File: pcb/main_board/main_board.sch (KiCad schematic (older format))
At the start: 32 parts, among them J1 Sensors_Conn, J2 Power_Conn, J3 I2C_Conn, J4 Garage_Conn, J5 Debug_Sensors_Conn, J6 Debug_I2C_Conn, U1 ESP-01, U2 HC_05, U3 AT24CS64-SSHM, U4 AMS1117-3.3, U5 Black_Pill

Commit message: PCB layout added
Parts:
- U1: footprint Connector_PinHeader_2.54mm:PinHeader_2x04_P2.54mm_Vertical -> project_footprints:ESP01
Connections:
- net DHT_SENSOR1: now also J1.6 (Pin_6), J5.6 (Pin_6); no longer J1.2 (Pin_2), J5.2 (Pin_2)
- net DHT_SENSOR2: now also J1.7 (Pin_7), J5.7 (Pin_7); no longer J1.3 (Pin_3), J5.3 (Pin_3)
- net DHT_SENSOR3: now also J1.2 (Pin_2), J5.2 (Pin_2); no longer J1.4 (Pin_4), J5.4 (Pin_4)
- net DHT_SENSOR4: now also J1.3 (Pin_3), J5.3 (Pin_3); no longer J1.5 (Pin_5), J5.5 (Pin_5)
- net DHT_SENSOR5: now also J1.4 (Pin_4), J5.4 (Pin_4); no longer J1.6 (Pin_6), J5.6 (Pin_6)
- net DHT_SENSOR6: now also J1.5 (Pin_5), J5.5 (Pin_5); no longer J1.7 (Pin_7), J5.7 (Pin_7)
- net I2C_INT: no longer J3.1 (Pin_1), J3.2 (Pin_2), J6.1 (Pin_1), J6.2 (Pin_2), R2.2, R3.2, U3.5 (SDA), U3.6 (SCL), U5.14 (B6), U5.15 (B7)
- new net I2C_SCL: J3.2 (Pin_2), J6.1 (Pin_1), R2.2, U3.6 (SCL), U5.14 (B6)
- new net I2C_SDA: J3.1 (Pin_1), J6.2 (Pin_2), R3.2, U3.5 (SDA), U5.15 (B7)
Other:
- moved on the sheet: C5, R1, R2, R3
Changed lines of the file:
@@
 Text GLabel 1750 2800 2    50   Input ~ 0
 5V
+Text GLabel 1750 2300 2    50   Input ~ 0
+DHT_SENSOR1
+Text GLabel 1750 2200 2    50   Input ~ 0
+DHT_SENSOR2
 Text GLabel 1750 2700 2    50   Input ~ 0
-DHT_SENSOR1
+DHT_SENSOR3
 Text GLabel 1750 2600 2    50   Input ~ 0
-DHT_SENSOR2
+DHT_SENSOR4
 Text GLabel 1750 2500 2    50   Input ~ 0
-DHT_SENSOR3
+DHT_SENSOR5
 Text GLabel 1750 2400 2    50   Input ~ 0
-DHT_SENSOR4
-Text GLabel 1750 2300 2    50   Input ~ 0
-DHT_SENSOR5
-Text GLabel 1750 2200 2    50   Input ~ 0
 DHT_SENSOR6
 Text GLabel 1750 2100 2    50   Input ~ 0
@@
 NoConn ~ 3000 2000
 NoConn ~ 3000 2100
-Text GLabel 3000 2200 2    50   Input ~ 0
-I2C_INT
-Text GLabel 3000 2300 2    50   Input ~ 0
-I2C_SCL
 $Comp
 L Connector:Conn_01x04_Female J4
@@
 Text GLabel 3000 2950 2    50   Input ~ 0
 GARAGE_RX_STM_TX
-$Comp
-L project_symbols:ESP-01 U1
-U 1 1 5FFDA57F
-P 2450 4000
-F 0 "U1" H 2450 4581 50  0000 C CNN
-F 1 "ESP-01" H 2450 4490 50  0000 C CNN
-F 2 "Connector_PinHeader_2.54mm:PinHeader_2x04_P2.54mm_Vertical" H 2450 4489 50  0001 C CNN
-F 3 "" H 2100 4100 50  0001 C CNN
-	1    2450 4000
-	1    0    0    -1
-$EndComp
 Text GLabel 2450 4450 3    50   Input ~ 0
 GND
@@
 Text GLabel 2500 6750 2    50   Input ~ 0
 3.3V
-Text GLabel 2900 7050 2    50   Input ~ 0
-I2C_SCL
-Text GLabel 2900 6950 2    50   Input ~ 0
-I2C_SDA
 Wire Notes Line
 	1350 6500 3850 6500
@@
 L Device:R R1
 U 1 1 6004496A
-P 5100 4450
-F 0 "R1" H 5170 4496 50  0000 L CNN
-F 1 "10k" H 5170 4405 50  0000 L CNN
-F 2 "Resistor_SMD:R_1206_3216Metric_Pad1.30x1.75mm_HandSolder" V 5030 4450 50  0001 C CNN
-F 3 "~" H 5100 4450 50  0001 C CNN
-	1    5100 4450
-	1    0    0    -1
-$EndComp
-Text GLabel 5100 4300 1    50   Input ~ 0
-5V
-Text GLabel 4800 4700 0    50   Input ~ 0
-I2C_SCL
+P 5100 4400
+F 0 "R1" H 5170 4446 50  0000 L CNN
+F 1 "10k" H 5170 4355 50  0000 L CNN
+F 2 "Resistor_SMD:R_1206_3216Metric_Pad1.30x1.75mm_HandSolder" V 5030 4400 50  0001 C CNN
+F 3 "~" H 5100 4400 50  0001 C CNN
+	1    5100 4400
+	1    0    0    -1
+$EndComp
+Text GLabel 5100 4250 1    50   Input ~ 0
+5V
 $Comp
 L Connector:Conn_01x06_Female J3
@@
 	-1   0    0    1
 $EndComp
-Text GLabel 3000 2400 2    50   Input ~ 0
-I2C_SDA
-Text GLabel 4800 4800 0    50   Input ~ 0
-I2C_SDA
 $Comp
 L Device:R R3
 U 1 1 6004C3D0
-P 5650 4450
-F 0 "R3" H 5720 4496 50  0000 L CNN
-F 1 "10k" H 5720 4405 50  0000 L CNN
-F 2 "Resistor_SMD:R_1206_3216Metric_Pad1.30x1.75mm_HandSolder" V 5580 4450 50  0001 C CNN
-F 3 "~" H 5650 4450 50  0001 C CNN
-	1    5650 4450
-	1    0    0    -1
-$EndComp
-Text GLabel 5350 4300 1    50   Input ~ 0
-5V
-Text GLabel 5650 4300 1    50   Input ~ 0
-5V
-Text GLabel 4800 4600 0    50   Input ~ 0
-I2C_INT
-Wire Wire Line
-	5350 4600 5350 4700
-Wire Wire Line
-	5650 4600 5650 4800
+P 5650 4400
+F 0 "R3" H 5720 4446 50  0000 L CNN
+F 1 "10k" H 5720 4355 50  0000 L CNN
+F 2 "Resistor_SMD:R_1206_3216Metric_Pad1.30x1.75mm_HandSolder" V 5580 4400 50  0001 C CNN
+F 3 "~" H 5650 4400 50  0001 C CNN
+	1    5650 4400
+	1    0    0    -1
+$EndComp
+Text GLabel 5350 4250 1    50   Input ~ 0
+5V
+Text GLabel 5650 4250 1    50   Input ~ 0
+5V
 $Comp
 L Device:R R5
@@
 Text GLabel 9150 4700 3    50   Input ~ 0
 GND
-Wire Wire Line
-	7400 4400 7700 4400
 Text GLabel 6600 4200 0    50   Input ~ 0
 GARAGE_TX_STM_RX
@@
 Wire Wire Line
 	4800 4600 4900 4600
-Connection ~ 5100 4600
 Wire Wire Line
 	4800 4700 5350 4700
@@
 L Device:C C5
 U 1 1 600B5AF0
-P 4900 4450
-F 0 "C5" H 4650 4500 50  0000 L CNN
-F 1 "47u" H 4650 4400 50  0000 L CNN
-F 2 "Capacitor_THT:CP_Radial_D8.0mm_P2.50mm" H 4938 4300 50  0001 C CNN
-F 3 "~" H 4900 4450 50  0001 C CNN
-	1    4900 4450
+P 4900 4400
+F 0 "C5" H 4650 4450 50  0000 L CNN
+F 1 "47u" H 4650 4350 50  0000 L CNN
+F 2 "Capacitor_THT:CP_Radial_D8.0mm_P2.50mm" H 4938 4250 50  0001 C CNN
+F 3 "~" H 4900 4400 50  0001 C CNN
+	1    4900 4400
 	1    0    0    -1
 $EndComp
 Connection ~ 4900 4600
-Wire Wire Line
-	4900 4600 5100 4600
-Text GLabel 4900 4300 1    50   Input ~ 0
-GND
-Wire Wire Line
-	5100 4600 5350 4600
+Text GLabel 4900 4250 1    50   Input ~ 0
+GND
 $Comp
 L Device:R R2
 U 1 1 6004B406
-P 5350 4450
-F 0 "R2" H 5420 4496 50  0000 L CNN
-F 1 "10k" H 5420 4405 50  0000 L CNN
-F 2 "Resistor_SMD:R_1206_3216Metric_Pad1.30x1.75mm_HandSolder" V 5280 4450 50  0001 C CNN
-F 3 "~" H 5350 4450 50  0001 C CNN
-	1    5350 4450
+P 5350 4400
+F 0 "R2" H 5420 4446 50  0000 L CNN
+F 1 "10k" H 5420 4355 50  0000 L CNN
+F 2 "Resistor_SMD:R_1206_3216Metric_Pad1.30x1.75mm_HandSolder" V 5280 4400 50  0001 C CNN
+F 3 "~" H 5350 4400 50  0001 C CNN
+	1    5350 4400
 	1    0    0    -1
 $EndComp
@@
 Text GLabel 10700 650  0    50   Input ~ 0
 5V
+Text GLabel 10700 1150 0    50   Input ~ 0
+DHT_SENSOR1
+Text GLabel 10700 1250 0    50   Input ~ 0
+DHT_SENSOR2
 Text GLabel 10700 750  0    50   Input ~ 0
-DHT_SENSOR1
+DHT_SENSOR3
 Text GLabel 10700 850  0    50   Input ~ 0
-DHT_SENSOR2
+DHT_SENSOR4
 Text GLabel 10700 950  0    50   Input ~ 0
-DHT_SENSOR3
+DHT_SENSOR5
 Text GLabel 10700 1050 0    50   Input ~ 0
-DHT_SENSOR4
-Text GLabel 10700 1150 0    50   Input ~ 0
-DHT_SENSOR5
-Text GLabel 10700 1250 0    50   Input ~ 0
 DHT_SENSOR6
 Text GLabel 10700 1350 0    50   Input ~ 0
@@
 	1    0    0    -1
 $EndComp
-Text GLabel 10700 2200 0    50   Input ~ 0
-I2C_INT
-Text GLabel 10700 2100 0    50   Input ~ 0
-I2C_SCL
-Text GLabel 10700 2000 0    50   Input ~ 0
-I2C_SDA
 Text GLabel 10700 2300 0    50   Input ~ 0
 GND
@@
 Text Notes 8300 1800 0    79   ~ 0
 Sensors PullUp
-Connection ~ 5350 4600
-Wire Wire Line
-	5350 4600 5650 4600
-Connection ~ 5650 4600
-Wire Wire Line
-	5650 4600 6250 4600
 Wire Notes Line
 	4200 2750 9650 2750
@@
 NoConn ~ 7400 5200
 NoConn ~ 12100 5900
+Text GLabel 10700 2200 0    50   Input ~ 0
+I2C_INT
+Text GLabel 10700 2000 0    50   Input ~ 0
+I2C_SCL
+Text GLabel 10700 2100 0    50   Input ~ 0
+I2C_SDA
+Text GLabel 2900 6950 2    50   Input ~ 0
+I2C_SDA
+Text GLabel 2900 7050 2    50   Input ~ 0
+I2C_SCL
+Text GLabel 4800 4800 0    50   Input ~ 0
+I2C_SDA
+Text GLabel 4800 4700 0    50   Input ~ 0
+I2C_SCL
+Text GLabel 4800 4600 0    50   Input ~ 0
+I2C_INT
+Text GLabel 3000 2200 2    50   Input ~ 0
+I2C_INT
+Text GLabel 3000 2400 2    50   Input ~ 0
+I2C_SDA
+Text GLabel 3000 2300 2    50   Input ~ 0
+I2C_SCL
+Wire Wire Line
+	4900 4600 5100 4600
+Wire Wire Line
+	4900 4550 4900 4600
+Wire Wire Line
+	5100 4550 5100 4600
+Connection ~ 5100 4600
+Wire Wire Line
+	5650 4550 5650 4800
+Wire Wire Line
+	5350 4550 5350 4700
+Wire Wire Line
+	5100 4600 6250 4600
+$Comp
+L project_symbols:ESP-01 U1
+U 1 1 5FFDA57F
+P 2450 4000
+F 0 "U1" H 2450 4581 50  0000 C CNN
+F 1 "ESP-01" H 2450 4490 50  0000 C CNN
+F 2 "project_footprints:ESP01" H 2450 4489 50  0001 C CNN
+F 3 "" H 2100 4100 50  0001 C CNN
+	1    2450 4000
+	1    0    0    -1
+$EndComp
+Wire Wire Line
+	7400 4400 7700 4400
 $EndSCHEMATC

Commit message: Main board PCB updated
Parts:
- J3: footprint Connector_IDC:IDC-Header_2x04_P2.54mm_Vertical -> Connector_IDC:IDC-Header_2x03_P2.54mm_Vertical
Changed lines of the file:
@@
 Title "SmartHouse MainBoard"
 Date "2021-01-10"
-Rev "0.1"
+Rev "1.0"
 Comp ""
 Comment1 "This schematic defines the main board of whole system."
@@
 F 0 "J3" H 2692 1675 50  0000 C CNN
 F 1 "I2C_Conn" H 2692 1766 50  0000 C CNN
-F 2 "Connector_IDC:IDC-Header_2x04_P2.54mm_Vertical" H 2800 2200 50  0001 C CNN
+F 2 "Connector_IDC:IDC-Header_2x03_P2.54mm_Vertical" H 2800 2200 50  0001 C CNN
 F 3 "~" H 2800 2200 50  0001 C CNN
 	1    2800 2200

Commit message: main_baord reworked to one-side board
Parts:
- U2: footprint Connector_PinSocket_2.54mm:PinSocket_1x06_P2.54mm_Horizontal -> project_footprints:HC_05
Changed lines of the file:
@@
 Wire Notes Line
 	1350 1450 1350 3150
-$Comp
-L project_symbols:HC_05 U2
-U 1 1 600163EE
-P 2450 5600
-F 0 "U2" H 2122 5646 50  0000 R CNN
-F 1 "HC_05" H 2122 5555 50  0000 R CNN
-F 2 "Connector_PinSocket_2.54mm:PinSocket_1x06_P2.54mm_Horizontal" H 2350 5600 50  0001 C CNN
-F 3 "" H 2100 5700 50  0001 C CNN
-	1    2450 5600
-	1    0    0    -1
-$EndComp
 NoConn ~ 2850 5750
 Wire Notes Line
@@
 Wire Wire Line
 	7400 4400 7700 4400
+$Comp
+L project_symbols:HC_05 U2
+U 1 1 600163EE
+P 2450 5600
+F 0 "U2" H 2122 5646 50  0000 R CNN
+F 1 "HC_05" H 2122 5555 50  0000 R CNN
+F 2 "project_footprints:HC_05" H 2350 5600 50  0001 C CNN
+F 3 "" H 2100 5700 50  0001 C CNN
+	1    2450 5600
+	1    0    0    -1
+$EndComp
 $EndSCHEMATC

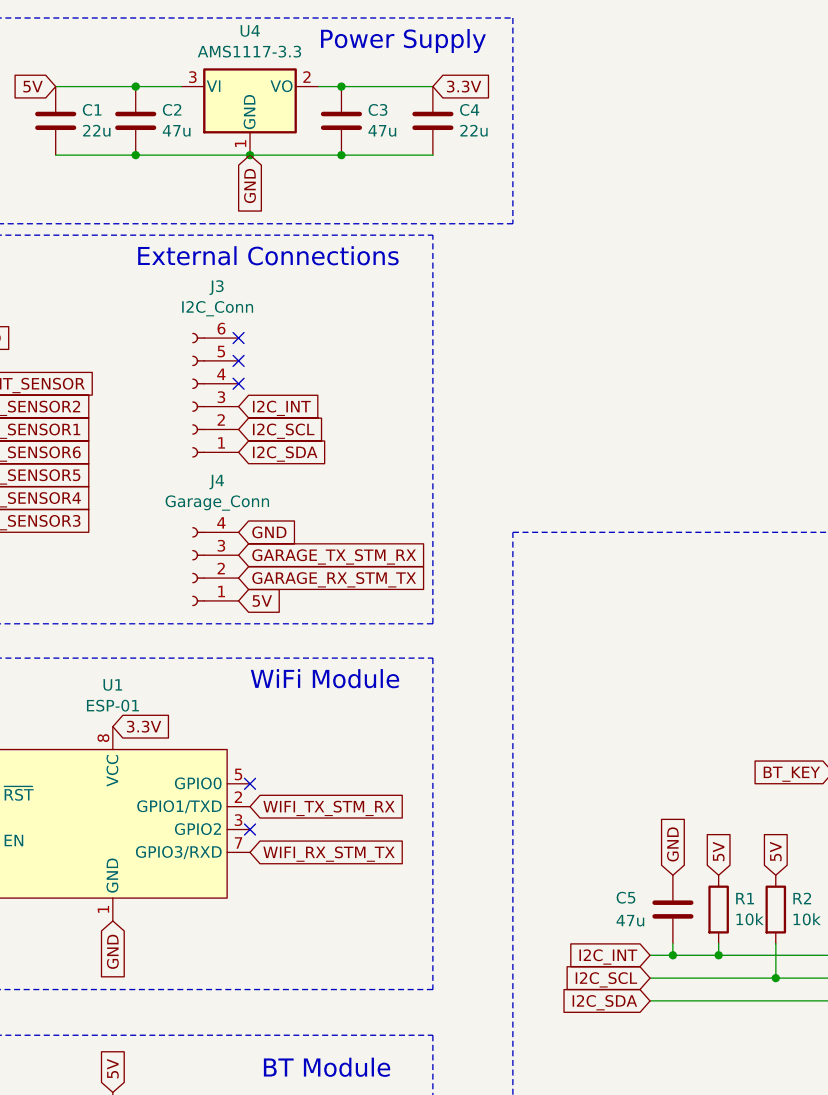
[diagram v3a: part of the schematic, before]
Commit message: Main board pcb updated
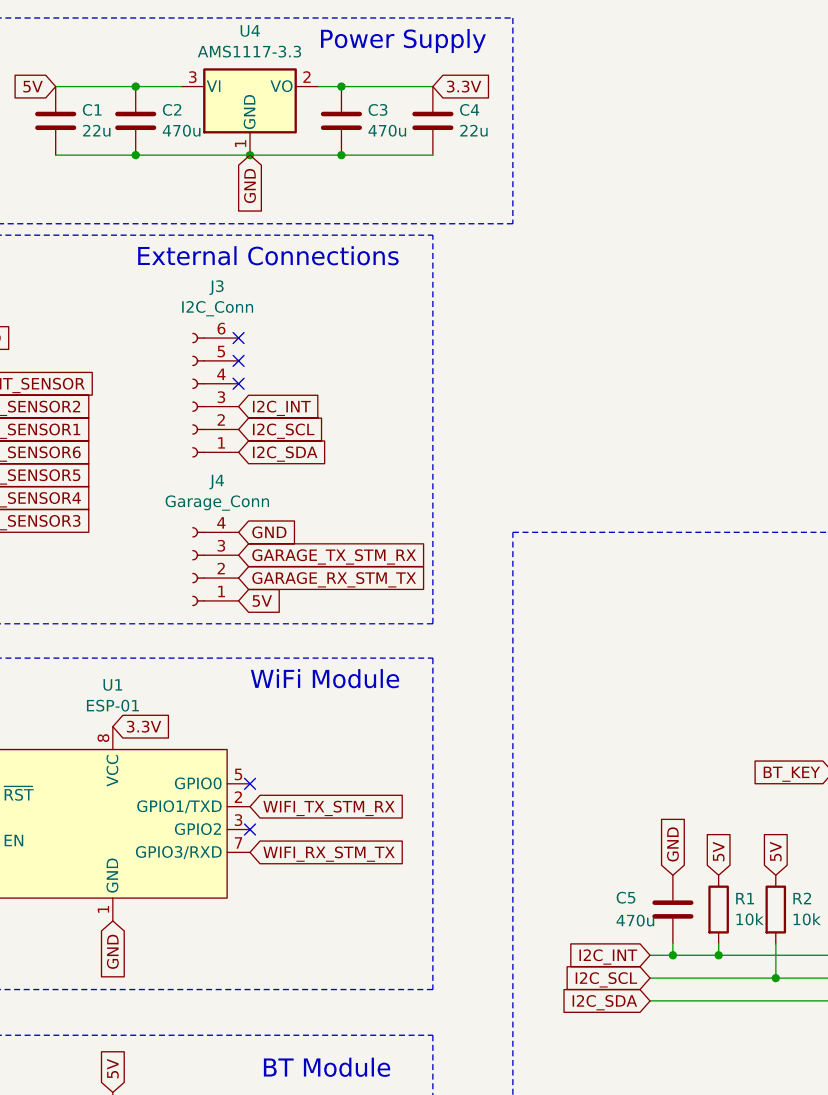
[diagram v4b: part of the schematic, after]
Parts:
- C2, C3, C5: value 47u -> 470u
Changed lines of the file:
@@
 P 2550 950
 F 0 "C2" H 2665 996 50  0000 L CNN
-F 1 "47u" H 2665 905 50  0000 L CNN
+F 1 "470u" H 2665 905 50  0000 L CNN
 F 2 "Capacitor_THT:CP_Radial_D8.0mm_P2.50mm" H 2588 800 50  0001 C CNN
 F 3 "~" H 2550 950 50  0001 C CNN
@@
 P 3450 950
 F 0 "C3" H 3565 996 50  0000 L CNN
-F 1 "47u" H 3565 905 50  0000 L CNN
+F 1 "470u" H 3565 905 50  0000 L CNN
 F 2 "Capacitor_THT:CP_Radial_D8.0mm_P2.50mm" H 3488 800 50  0001 C CNN
 F 3 "~" H 3450 950 50  0001 C CNN
@@
 P 4900 4400
 F 0 "C5" H 4650 4450 50  0000 L CNN
-F 1 "47u" H 4650 4350 50  0000 L CNN
+F 1 "470u" H 4650 4350 50  0000 L CNN
 F 2 "Capacitor_THT:CP_Radial_D8.0mm_P2.50mm" H 4938 4250 50  0001 C CNN
 F 3 "~" H 4900 4400 50  0001 C CNN
